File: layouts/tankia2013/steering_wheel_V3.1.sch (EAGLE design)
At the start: 92 parts, among them J1 1-292227-6, J2 1-292227-6, K1 USB-MICROZX62R-B, Q1 25 MHz, T1 FDC5614P, U1 STM32F415RG, U2 LMZ21701, U3 LMZ21701, U4 MAX6818, U5 NUF2221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

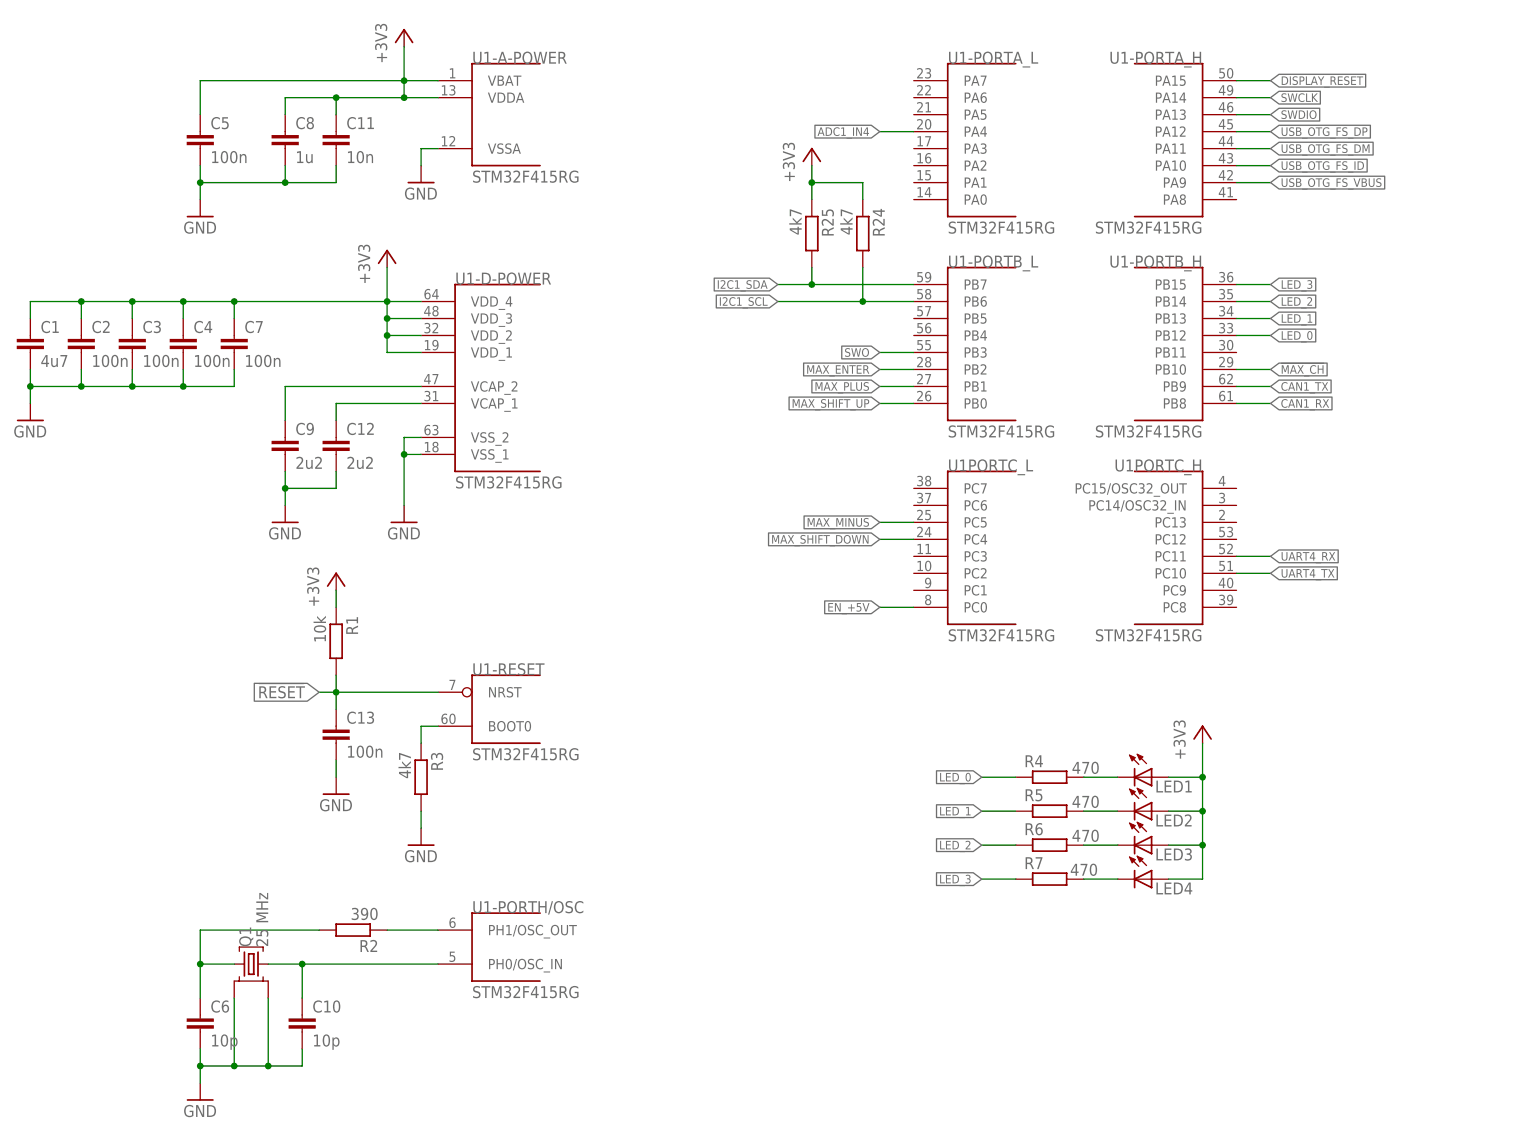
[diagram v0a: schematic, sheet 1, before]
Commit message: added stm32f7 breakout board
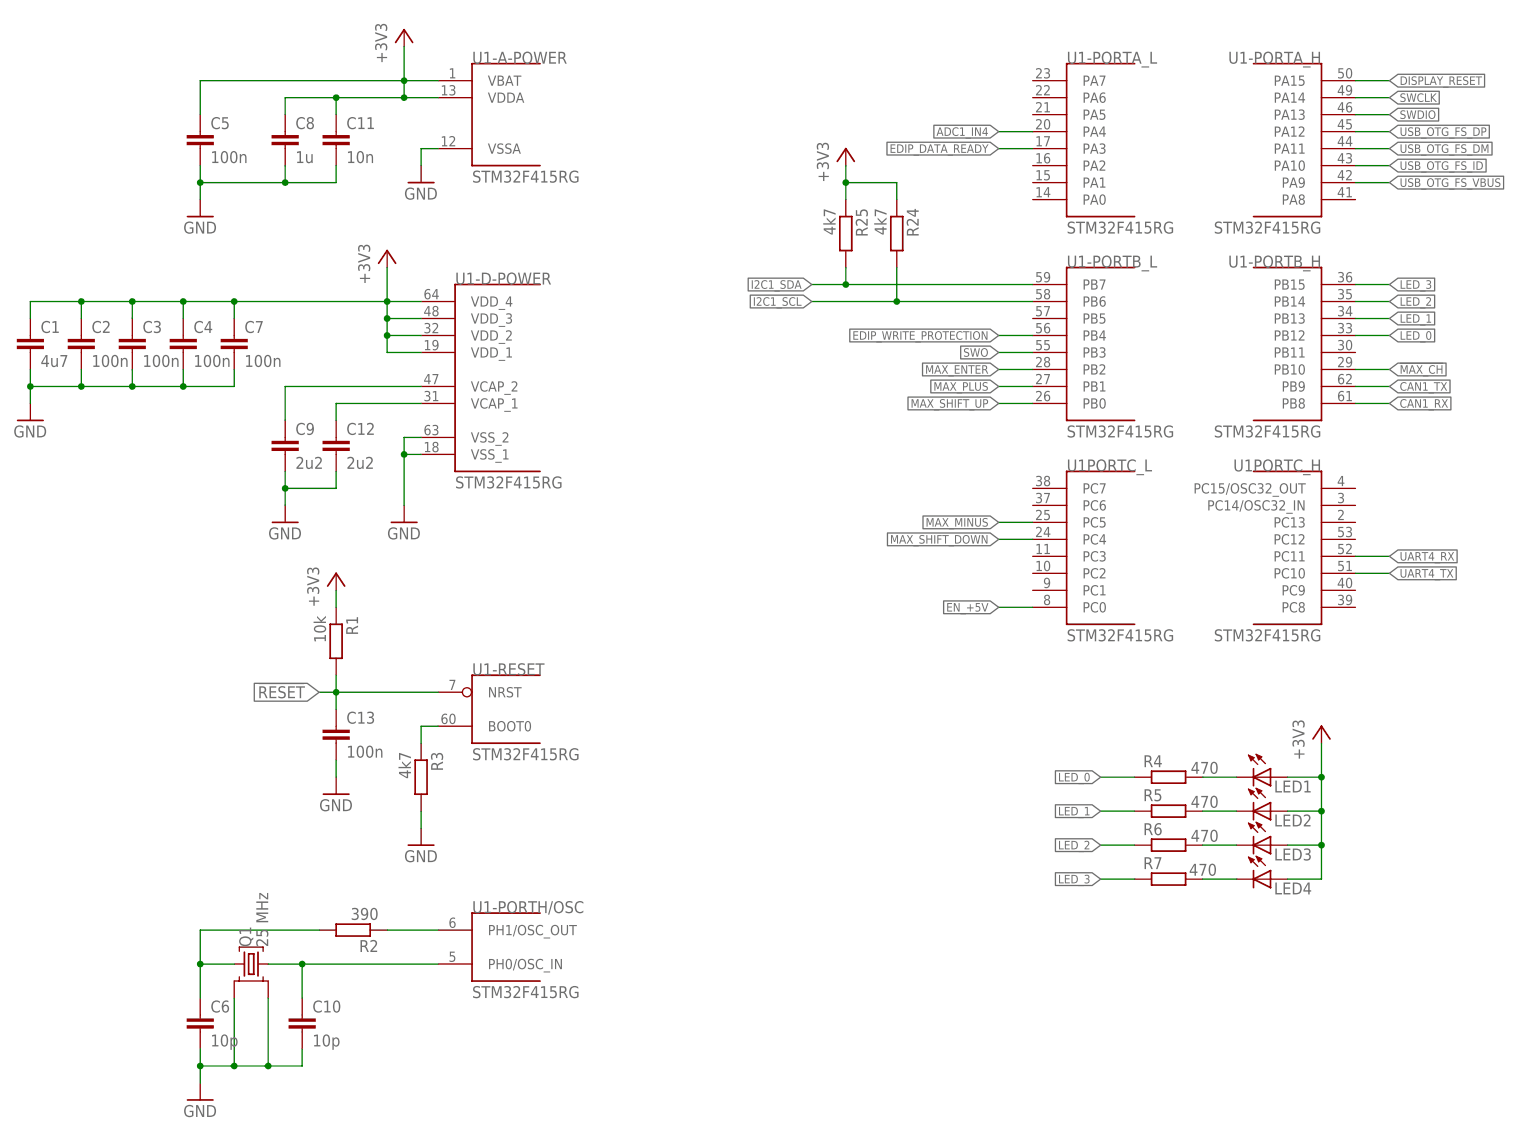
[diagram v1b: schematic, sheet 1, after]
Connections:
- new net EDIP_DATA_READY: DISPLAY.TEST_SBUF, U1-PORTA_L.PA3
- new net EDIP_WRITE_PROTECTION: DISPLAY.WP, U1-PORTB_L.PB4
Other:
- moved on the sheet: LED1, LED2, LED3, LED4, R24, R25, R4, R5, R6, R7, U1-PORTA_H, U1-PORTA_L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

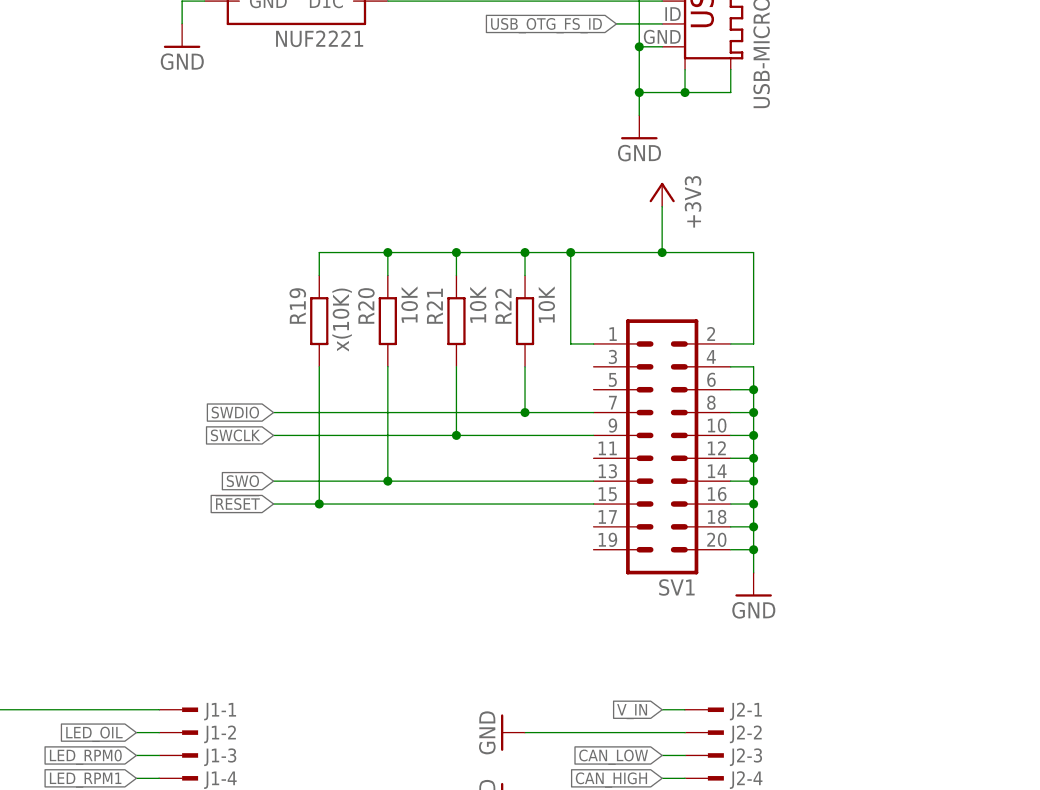
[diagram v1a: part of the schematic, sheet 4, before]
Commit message: updated layout, changed old 20 pin IDC to new 10 pin debug
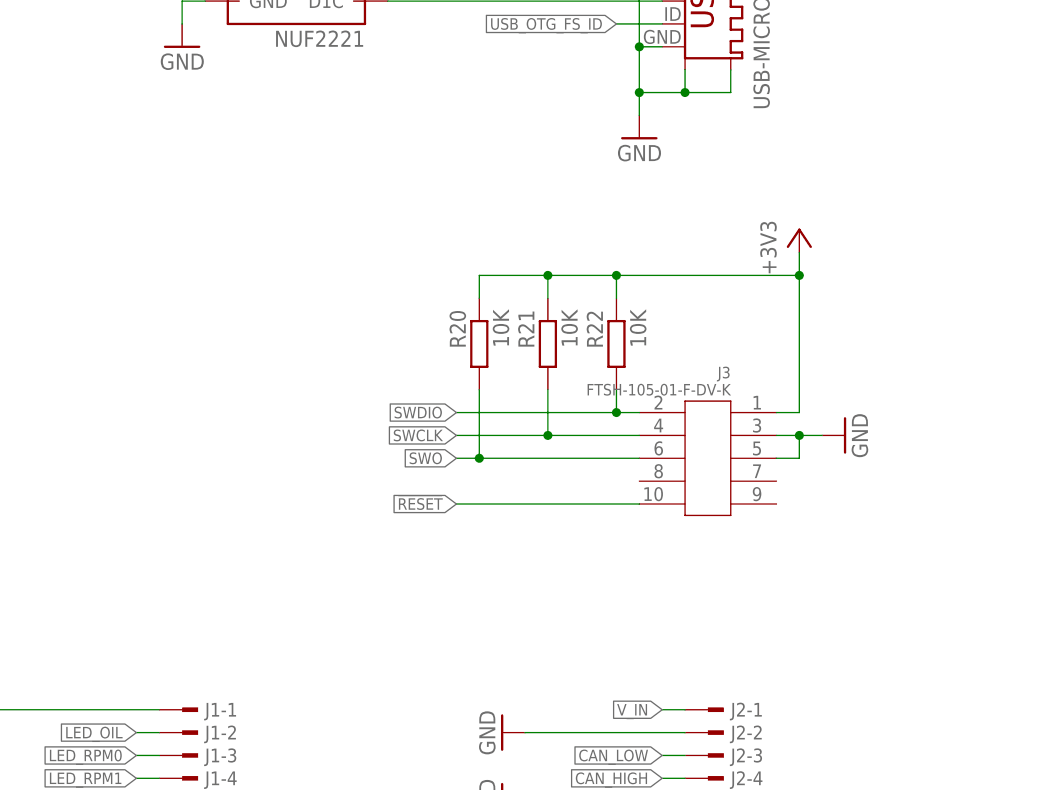
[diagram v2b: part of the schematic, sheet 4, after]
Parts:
- removed R19: x(10K), rcl:R-EU_R0603
- removed SV1: (no value), con-ml:ML20
- added J3: FTSH-105-01-F-DV-K, samtec:FTSH-105-01-F-DV-K
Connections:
- net !RESET: now also J3.10; no longer R19.2, SV1.15
- net +3V3: now also J3.1; no longer R19.1, SV1.1, SV1.2
- net GND: now also J3.3, J3.5; no longer SV1.10, SV1.12, SV1.14, SV1.16, SV1.18, SV1.20, SV1.4, SV1.6, SV1.8
- net SWCLK: now also J3.4; no longer SV1.9
- net SWDIO: now also J3.2; no longer SV1.7
- net SWO: now also J3.6; no longer SV1.13
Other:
- moved on the sheet: R20, R21, R22
